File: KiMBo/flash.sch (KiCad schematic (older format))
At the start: 20 parts

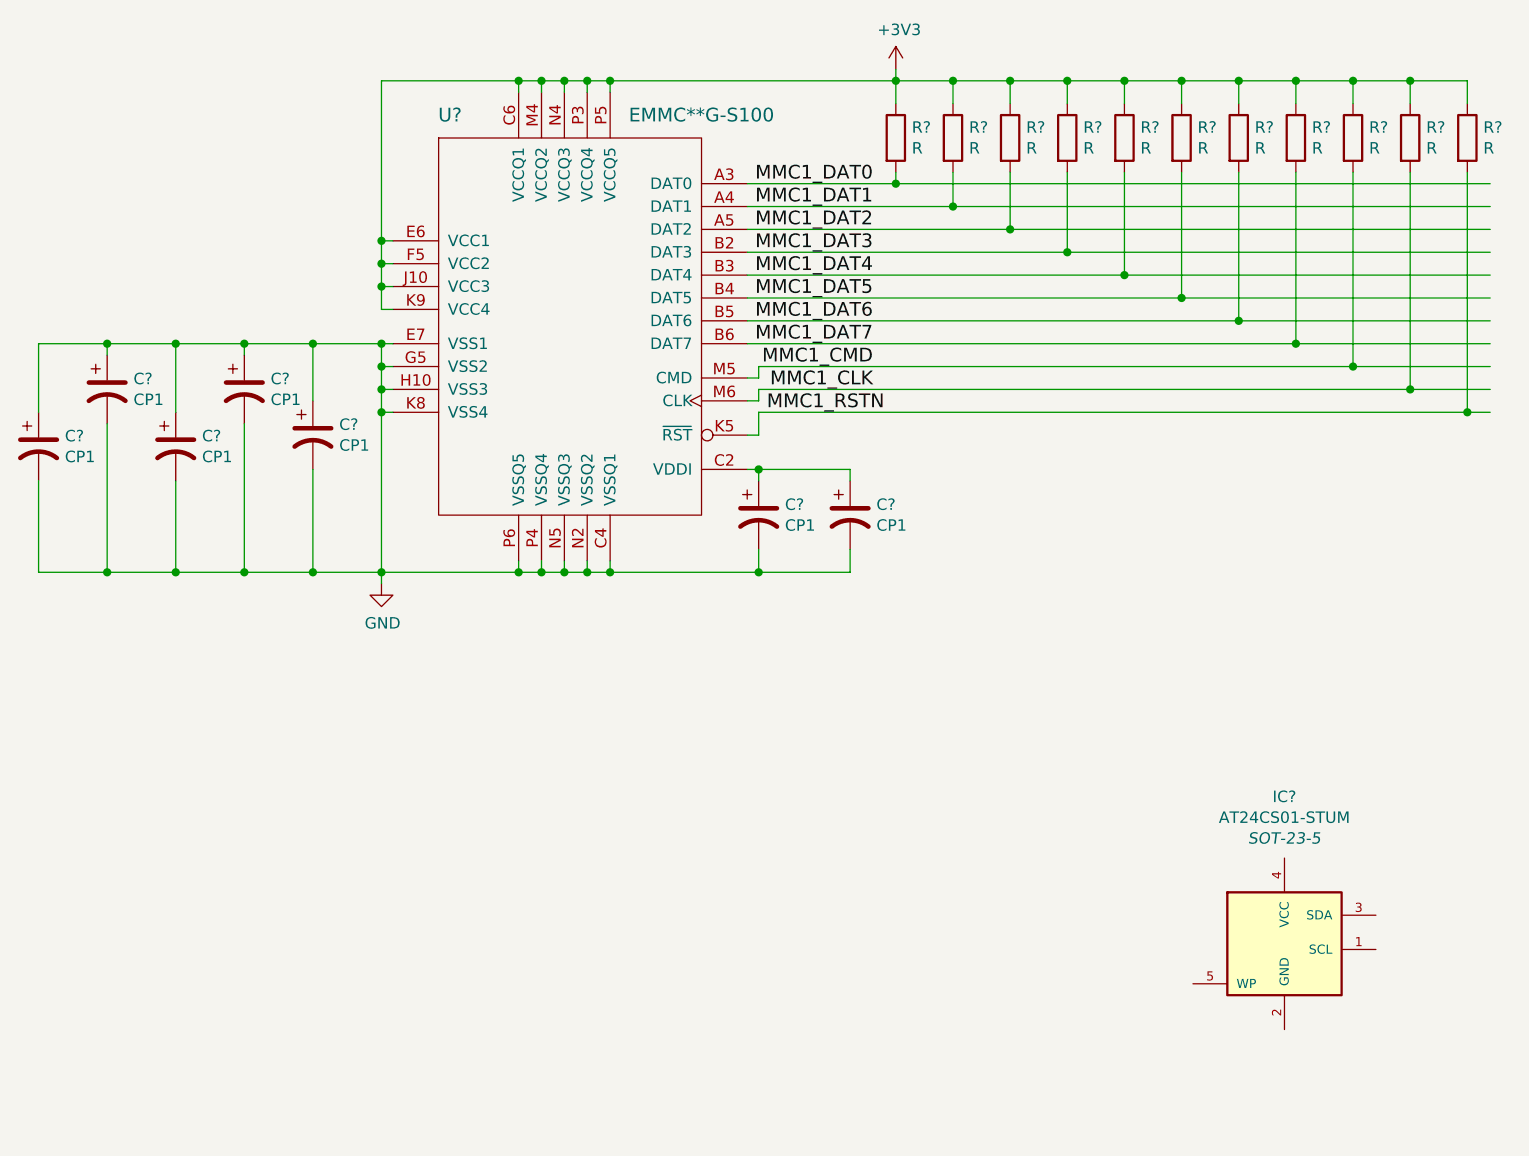
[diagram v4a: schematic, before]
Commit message: Use the TMC2130 stepper driver, document and calculate the stepper motor current
The current to the motors are set by IRUN and IHOLD of the IHOLD_IRUN register
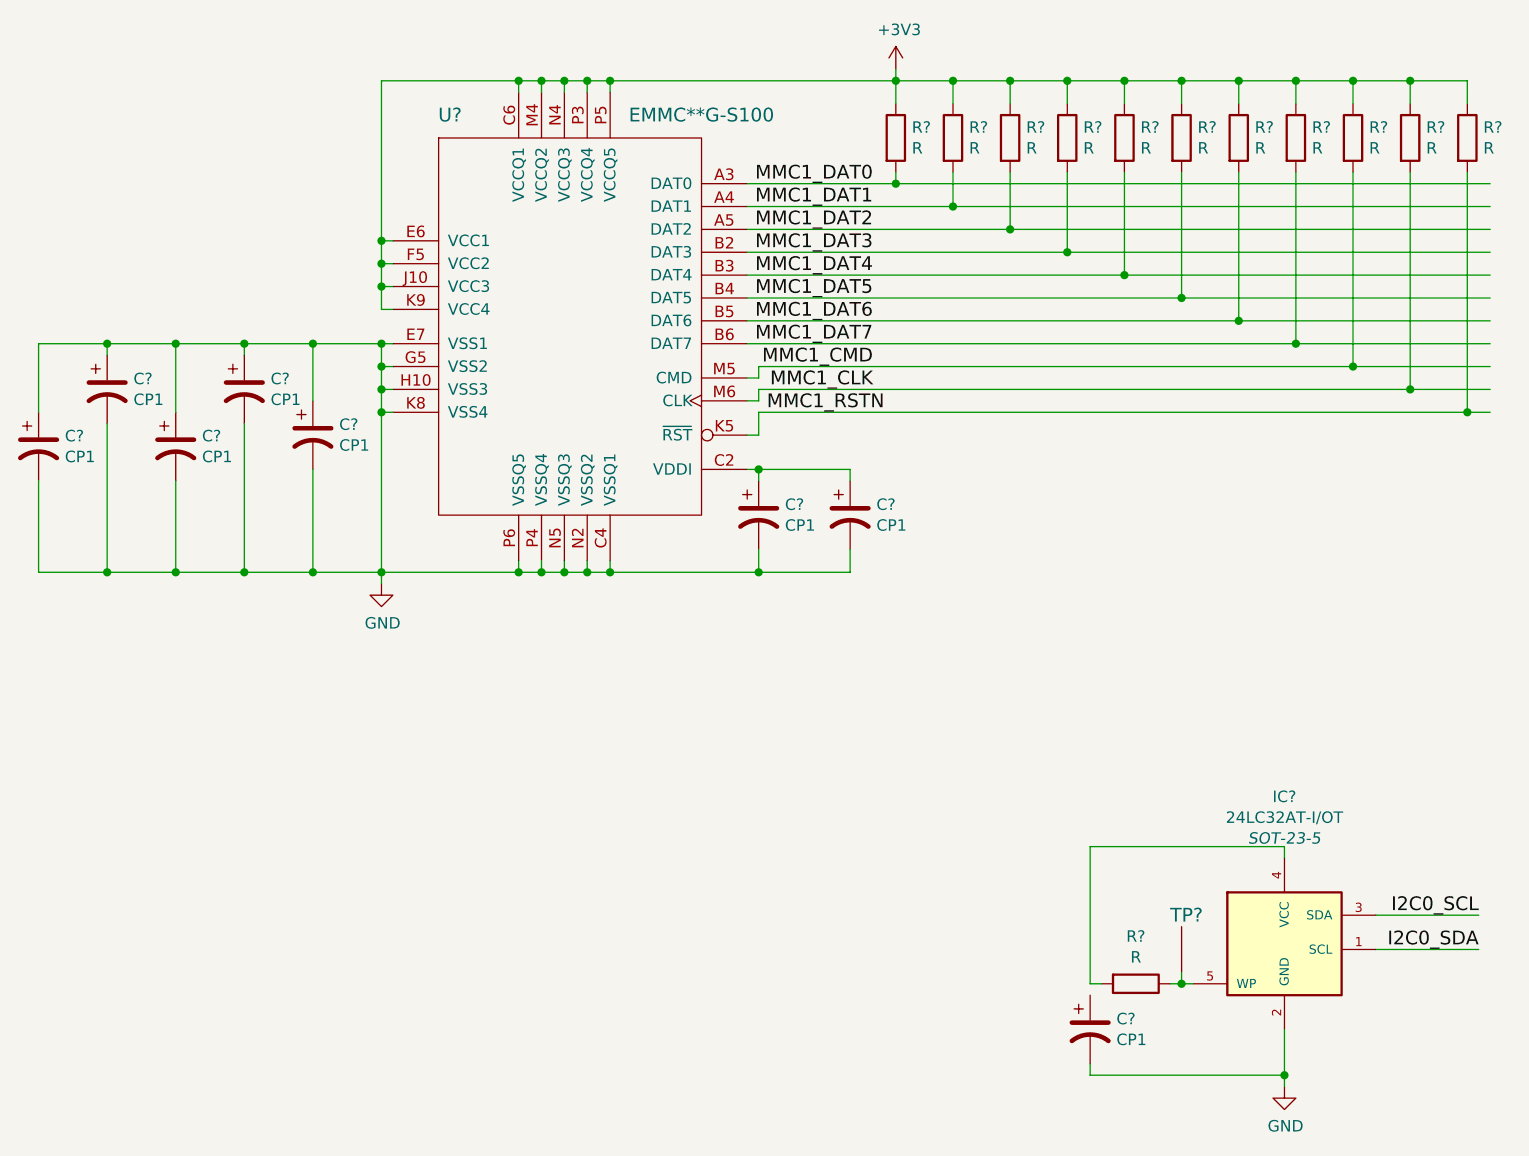
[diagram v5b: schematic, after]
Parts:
- added C?: CP1, symbol CP1
- added R?: R, symbol R
- added TP?: TP, symbol TP
- IC?: value AT24CS01-STUM -> 24LC32AT-I/OT
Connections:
- net labels added: I2C0_SCL, I2C0_SDA
- wire segments 127 -> 87
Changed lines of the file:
@@
 $Descr A3 16535 11693
 encoding utf-8
-Sheet 6 20
+Sheet 6 23
 Title ""
 Date ""
@@
 $EndComp
 Wire Wire Line
-	7350 3750 7350 4450
-Wire Wire Line
-	7350 4450 7350 4550
-Wire Wire Line
-	7350 4550 7350 4650
-Wire Wire Line
-	7350 4650 7350 4750
-Wire Wire Line
-	7350 3750 7950 3750
-Wire Wire Line
-	7950 3750 8050 3750
-Wire Wire Line
-	8050 3750 8150 3750
-Wire Wire Line
-	8150 3750 8250 3750
-Wire Wire Line
-	8250 3750 8350 3750
-Wire Wire Line
-	8350 3750 9600 3750
-Wire Wire Line
-	9600 3750 9850 3750
-Wire Wire Line
-	9850 3750 10100 3750
-Wire Wire Line
-	10100 3750 10350 3750
-Wire Wire Line
-	10350 3750 10600 3750
-Wire Wire Line
-	10600 3750 10850 3750
-Wire Wire Line
-	10850 3750 11100 3750
-Wire Wire Line
-	11100 3750 11350 3750
-Wire Wire Line
-	11350 3750 11600 3750
-Wire Wire Line
-	11600 3750 11850 3750
-Wire Wire Line
-	11850 3750 12100 3750
+	7350 3750 7350 4750
+Wire Wire Line
+	7350 3750 12100 3750
 Wire Wire Line
 	7400 4450 7350 4450
@@
 	8350 3750 8350 3800
 Wire Wire Line
-	7350 4900 7350 5000
-Wire Wire Line
-	7350 5000 7350 5100
-Wire Wire Line
-	7350 5100 7350 5200
-Wire Wire Line
-	7350 5200 7350 5900
-Wire Wire Line
-	7350 5900 7350 5950
-Wire Wire Line
-	5850 5900 6150 5900
-Wire Wire Line
-	6150 5900 6450 5900
-Wire Wire Line
-	6450 5900 6750 5900
-Wire Wire Line
-	6750 5900 7050 5900
-Wire Wire Line
-	7050 5900 7350 5900
-Wire Wire Line
-	7350 5900 7950 5900
-Wire Wire Line
-	7950 5900 8050 5900
-Wire Wire Line
-	8050 5900 8150 5900
-Wire Wire Line
-	8150 5900 8250 5900
-Wire Wire Line
-	8250 5900 8350 5900
-Wire Wire Line
-	8350 5900 9000 5900
-Wire Wire Line
-	9000 5900 9400 5900
-Wire Wire Line
-	5850 4900 6150 4900
-Wire Wire Line
-	6150 4900 6450 4900
-Wire Wire Line
-	6450 4900 6750 4900
-Wire Wire Line
-	6750 4900 7050 4900
-Wire Wire Line
-	7050 4900 7350 4900
-Wire Wire Line
-	7350 4900 7400 4900
+	7350 4900 7350 5950
+Wire Wire Line
+	5850 5900 9400 5900
+Wire Wire Line
+	5850 4900 7400 4900
 Wire Wire Line
 	7400 5000 7350 5000
@@
 $EndComp
 Wire Wire Line
-	8950 4200 9600 4200
-Wire Wire Line
-	9600 4200 12200 4200
+	8950 4200 12200 4200
 Wire Wire Line
 	9600 4200 9600 4150
@@
 $EndComp
 Wire Wire Line
-	8950 4300 9850 4300
-Wire Wire Line
-	9850 4300 12200 4300
+	8950 4300 12200 4300
 Wire Wire Line
 	9850 4300 9850 4150
 Wire Wire Line
-	8950 4400 10100 4400
-Wire Wire Line
-	10100 4400 12200 4400
+	8950 4400 12200 4400
 Wire Wire Line
 	10100 4400 10100 4150
 Wire Wire Line
-	8950 4500 10350 4500
-Wire Wire Line
-	10350 4500 12200 4500
+	8950 4500 12200 4500
 Wire Wire Line
 	10350 4500 10350 4150
 Wire Wire Line
-	8950 4600 10600 4600
-Wire Wire Line
-	10600 4600 12200 4600
+	8950 4600 12200 4600
 Wire Wire Line
 	10600 4600 10600 4150
 Wire Wire Line
-	8950 4700 10850 4700
-Wire Wire Line
-	10850 4700 12200 4700
+	8950 4700 12200 4700
 Wire Wire Line
 	10850 4700 10850 4150
 Wire Wire Line
-	8950 4800 11100 4800
-Wire Wire Line
-	11100 4800 12200 4800
+	8950 4800 12200 4800
 Wire Wire Line
 	11100 4800 11100 4150
 Wire Wire Line
-	8950 4900 11350 4900
-Wire Wire Line
-	11350 4900 12200 4900
+	8950 4900 12200 4900
 Wire Wire Line
 	11350 4900 11350 4150
 Wire Wire Line
-	9000 5000 11600 5000
-Wire Wire Line
-	11600 5000 12200 5000
+	9000 5000 12200 5000
 Wire Wire Line
 	11600 5000 11600 4150
@@
 Connection ~ 8350 3750
 Wire Wire Line
-	9600 3700 9600 3750
-Wire Wire Line
-	9600 3750 9600 3850
+	9600 3700 9600 3850
 Connection ~ 9600 3750
 Wire Wire Line
@@
 	9000 5500 9000 5450
 Wire Wire Line
-	8950 5450 9000 5450
-Wire Wire Line
-	9000 5450 9400 5450
+	8950 5450 9400 5450
 Wire Wire Line
 	9400 5450 9400 5500
@@
 	9000 5150 9000 5100
 Wire Wire Line
-	9000 5100 11850 5100
-Wire Wire Line
-	11850 5100 12200 5100
+	9000 5100 12200 5100
 Wire Wire Line
 	8950 5300 9000 5300
@@
 	9000 5300 9000 5200
 Wire Wire Line
-	9000 5200 12100 5200
-Wire Wire Line
-	12100 5200 12200 5200
+	9000 5200 12200 5200
 Wire Wire Line
 	12100 5200 12100 4150
@@
 P 11300 7500
 F 0 "IC?" H 11300 8118 50  0000 C CNN
-F 1 "AT24CS01-STUM" H 11300 8027 50  0000 C CNN
+F 1 "24LC32AT-I/OT" H 11300 8027 50  0000 C CNN
 F 2 "SOT-23-5" H 11300 7936 50  0000 C CIN
 F 3 "" H 11300 7500 50  0000 C CNN
@@
 	1    0    0    -1
 $EndComp
+$Comp
+L R R?
+U 1 1 589CA43D
+P 10650 7700
+F 0 "R?" V 10443 7700 50  0000 C CNN
+F 1 "R" V 10534 7700 50  0000 C CNN
+F 2 "" V 10580 7700 50  0000 C CNN
+F 3 "" H 10650 7700 50  0000 C CNN
+	1    10650 7700
+	0    1    1    0
+$EndComp
+$Comp
+L TP TP?
+U 1 1 589CA4A3
+P 10850 7650
+F 0 "TP?" V 11100 7700 60  0000 R CNN
+F 1 "TP" H 10850 7600 60  0001 C CNN
+F 2 "" H 10850 7650 60  0000 C CNN
+F 3 "" H 10850 7650 60  0000 C CNN
+	1    10850 7650
+	0    -1   -1   0
+$EndComp
+Wire Wire Line
+	10850 7650 10850 7700
+Wire Wire Line
+	10800 7700 10900 7700
+Connection ~ 10850 7700
+Wire Wire Line
+	11300 7150 11300 7100
+Wire Wire Line
+	11300 7100 10450 7100
+Wire Wire Line
+	10450 7100 10450 7700
+Wire Wire Line
+	10450 7700 10500 7700
+$Comp
+L CP1 C?
+U 1 1 589CA9AC
+P 10450 7900
+F 0 "C?" H 10565 7946 50  0000 L CNN
+F 1 "CP1" H 10565 7855 50  0000 L CNN
+F 2 "" H 10450 7900 50  0000 C CNN
+F 3 "" H 10450 7900 50  0000 C CNN
+	1    10450 7900
+	1    0    0    -1
+$EndComp
+Wire Wire Line
+	11300 7900 11300 8150
+Wire Wire Line
+	11300 8100 10450 8100
+Wire Wire Line
+	10450 8100 10450 8050
+$Comp
+L GND #PWR?
+U 1 1 589CAA98
+P 11300 8150
+F 0 "#PWR?" H 11300 7900 50  0001 C CNN
+F 1 "GND" H 11305 7977 50  0000 C CNN
+F 2 "" H 11300 8150 50  0000 C CNN
+F 3 "" H 11300 8150 50  0000 C CNN
+	1    11300 8150
+	1    0    0    -1
+$EndComp
+Connection ~ 11300 8100
+Text Label 12150 7400 2    60   ~ 0
+I2C0_SCL
+Text Label 12150 7550 2    60   ~ 0
+I2C0_SDA
+Wire Wire Line
+	12150 7400 11700 7400
+Wire Wire Line
+	12150 7550 11700 7550
 $EndSCHEMATC

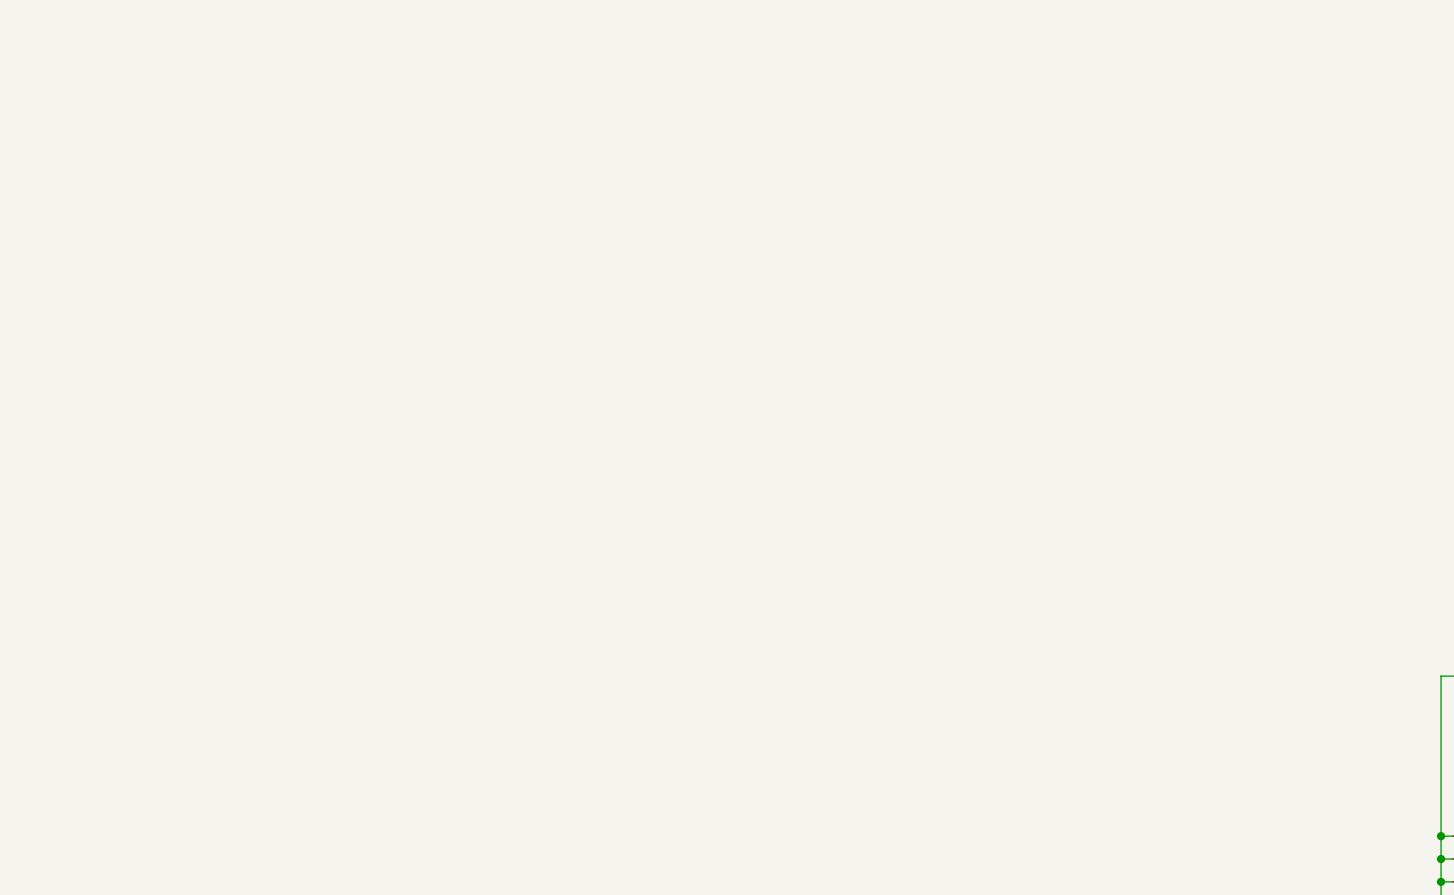
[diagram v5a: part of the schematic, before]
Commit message: Bring more interfaces out to the root sheet and begin connecting modules
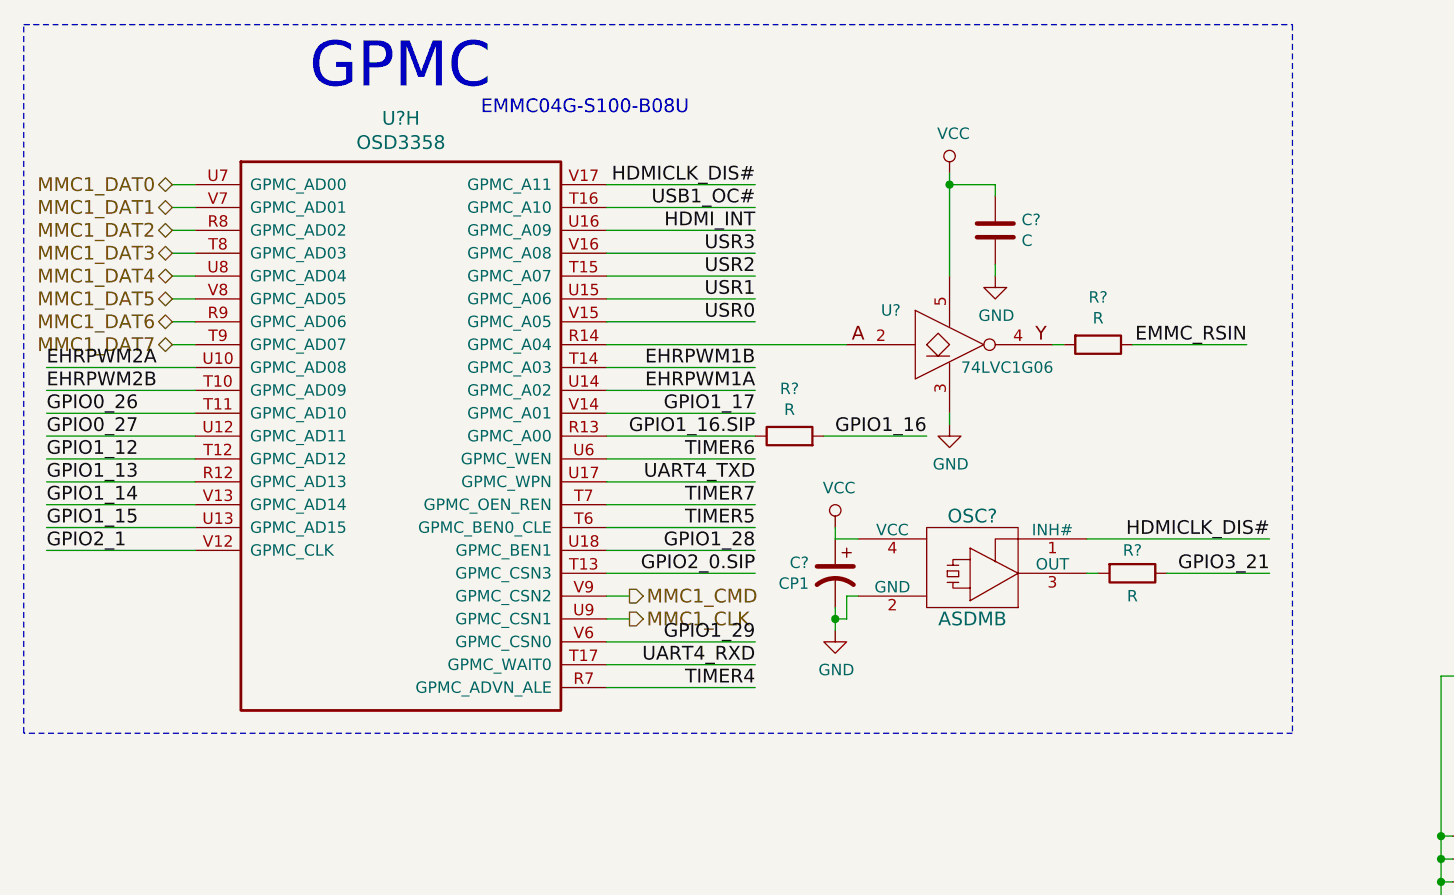
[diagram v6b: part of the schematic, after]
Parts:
- added C?: C, symbol C
- added C?: CP1, symbol CP1
- added OSC?: ASDMB, symbol ASDMB
- added R? (x3): R, symbol R
- added U?: OSD3358, symbol OSD3358
- added U?: 74LVC1G06, symbol 74LVC1G06
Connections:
- net labels added: EHRPWM1A, EHRPWM1B, EHRPWM2A, EHRPWM2B, EMMC_RSIN, GPIO0_26, GPIO0_27, GPIO1_12, GPIO1_13, GPIO1_14, GPIO1_15, GPIO1_16, GPIO1_16.SIP, GPIO1_17, GPIO1_28, GPIO1_29, GPIO2_0.SIP, GPIO2_1, GPIO3_21, HDMICLK_DIS#, HDMI_INT, TIMER4, TIMER5, TIMER6, TIMER7, UART4_RXD, UART4_TXD, USB1_OC#, USR0, USR1, USR2, USR3, VCC
- wire segments 87 -> 144
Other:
- note added: "EMMC04G-S100-B08U"
- note added: "GPMC"
